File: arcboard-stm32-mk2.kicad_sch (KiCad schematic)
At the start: 92 parts, among them J1 Conn_01x04_Socket, J17 Conn_01x04_Socket, J2 Conn_01x04_Socket, J3 Conn_01x04_Socket, J4 Conn_01x02_Socket, J5 Conn_01x02_Socket, J6 Conn_01x02_Socket, J7 Conn_01x02_Socket, J8 Conn_01x02_Socket, U1 XC6210B332MR-G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

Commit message: refactoring rgb-lcd power to match tzarc, old way was fundamentally broken
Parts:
- removed JP1, JP4: SolderJumper_3_Open, Jumper:SolderJumper-3_P1.3mm_Open_RoundedPad1.0x1.5mm, symbol Jumper:SolderJumper_3_Open
- removed MOSFET2: AO3401A, kicad-libraries:SOT-23_L2.9-W1.3-P1.90-LS2.4-BR, symbol kicad-libraries:AO3401A
- removed R7, R8: 10k, Resistor_SMD:R_0402_1005Metric, symbol Device:R
- added MOSFET4: AO3401A, kicad-libraries:SOT-23_L2.9-W1.3-P1.90-LS2.4-BR, symbol kicad-libraries:AO3401A
- added U10, U9: MMUN2233LT1G, kicad-libraries:SOT-23-3_L2.9-W1.3-P1.90-LS2.4-BR, symbol kicad-libraries:MMUN2233LT1G
- D1: LCSC (none) -> C8678
- J4, J8, U7: now left out of the parts list
- U2: LCSC (none) -> C12345
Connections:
- net +5V: now also MOSFET4.2 (S)
- net GND: now also U10.2 (E), U9.2 (E)
- net LCD_ON: now also U9.1 (B)
- net RGB_5V: now also MOSFET4.3 (D)
- net RGB_ON: now also U10.1 (B)
- net at MOSFET3.1 (G): now also U9.3 (C)
- new net: MOSFET4.1 (G), U10.3 (C)
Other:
- note removed: "v1.1: Moved from 8mhz to 12mhz crystal, to satisfy QMK defaults."
- moved on the sheet: MOSFET3, Y1

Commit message: silkscreen refactoring and moving bits around
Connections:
- no-connect marks 34 -> 36
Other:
- moved on the sheet: MOSFET3, MOSFET4, U10, U9

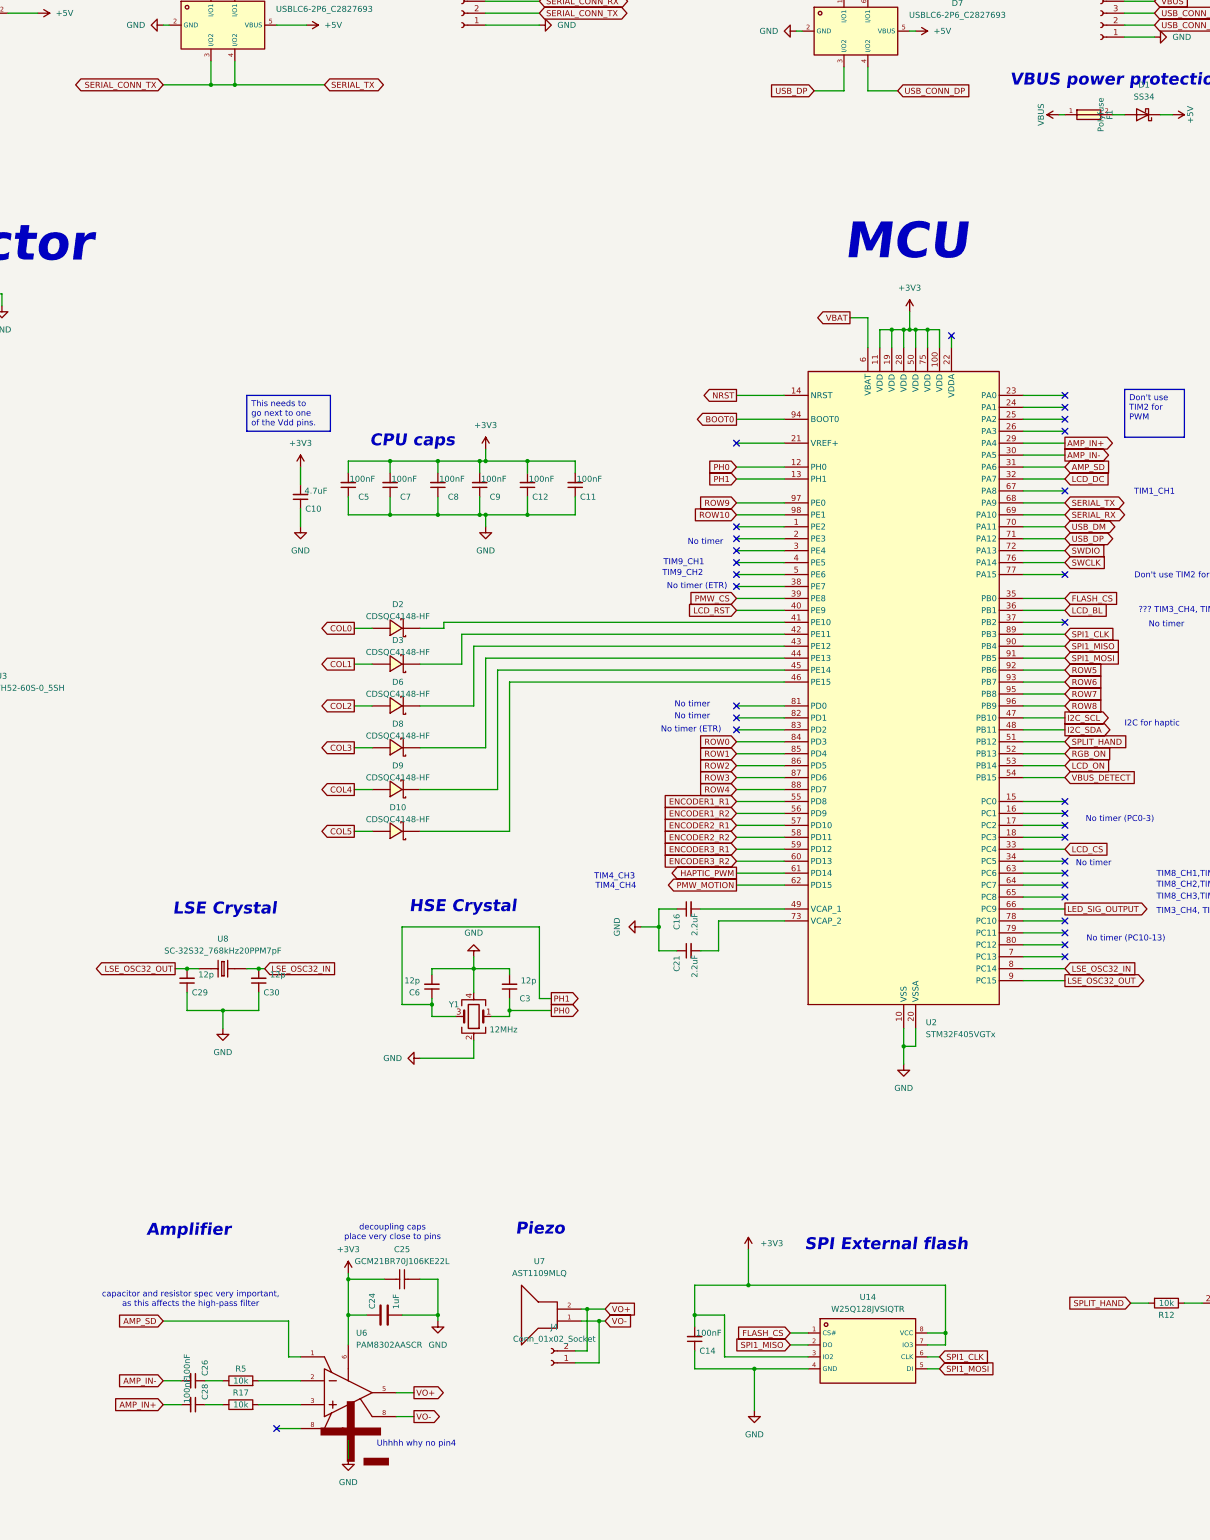
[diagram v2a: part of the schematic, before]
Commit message: improved polyfuse part, fixing critical amplifier symbol mistake, other re-ordering
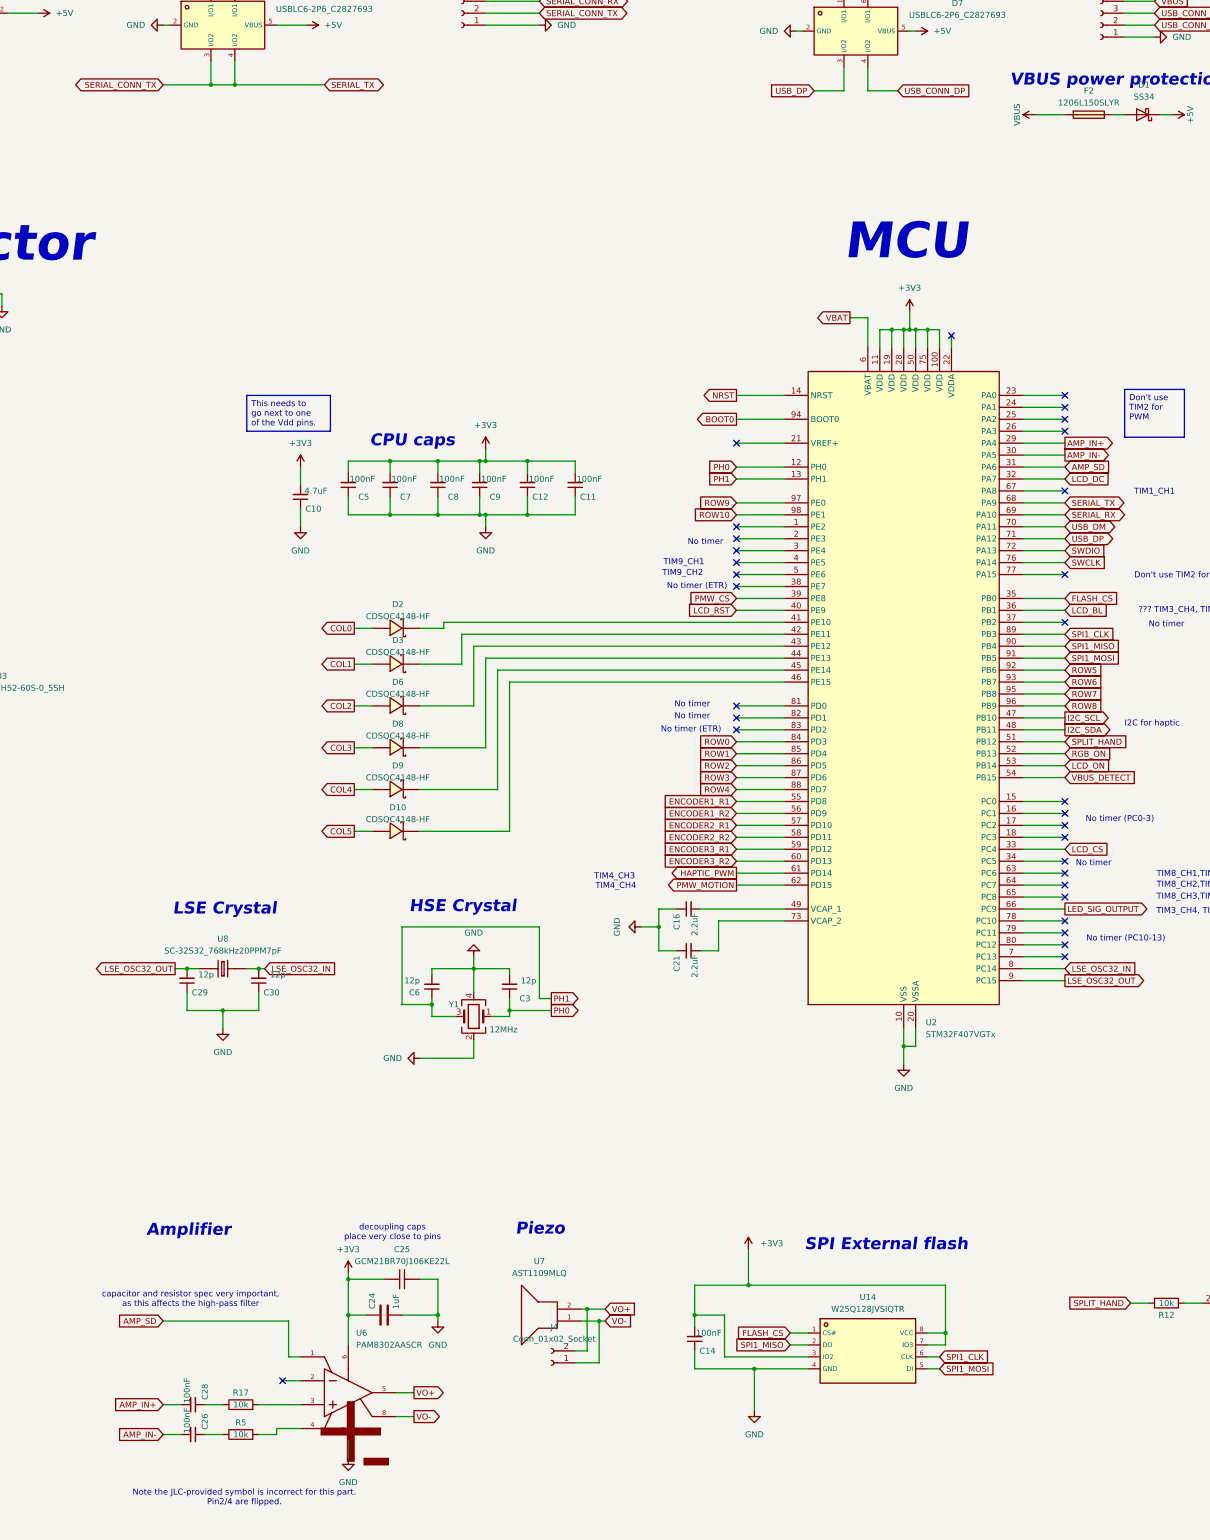
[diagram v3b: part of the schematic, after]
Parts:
- removed F1: Polyfuse, kicad-libraries:F1206, symbol ct-kicad:RF1989-000
- added F2: 1206L150SLYR, kicad-libraries:F1206, symbol kicad-libraries:1206L150SLYR
- U2: value STM32F405VGTx -> STM32F407VGTx
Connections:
- net VBUS: now also F2.1
- net at D1.2 (A): now also F2.2
- net at R5.2: now also U6.4 (IN-); no longer U6.2 (IN-)
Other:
- note added: "Note the JLC-provided symbol is incorrect for this part. Pin2/4 are flipped."
- note removed: "Uhhhh why no pin4"
- moved on the sheet: C26, R5

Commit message: almost ready for ordering
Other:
- note added: "TIM3_CH4, TIM8_CH3N, TIM1_CH3N"
- note removed: "??? TIM3_CH4, TIM8_CH3N, TIM1_CH3N"
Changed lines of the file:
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@@
 		)
 	)
-	(text "??? TIM3_CH4, TIM8_CH3N, TIM1_CH3N"
+	(text "TIM3_CH4, TIM8_CH3N, TIM1_CH3N"
 		(exclude_from_sim no)
 		(at 379.476 204.47 0)

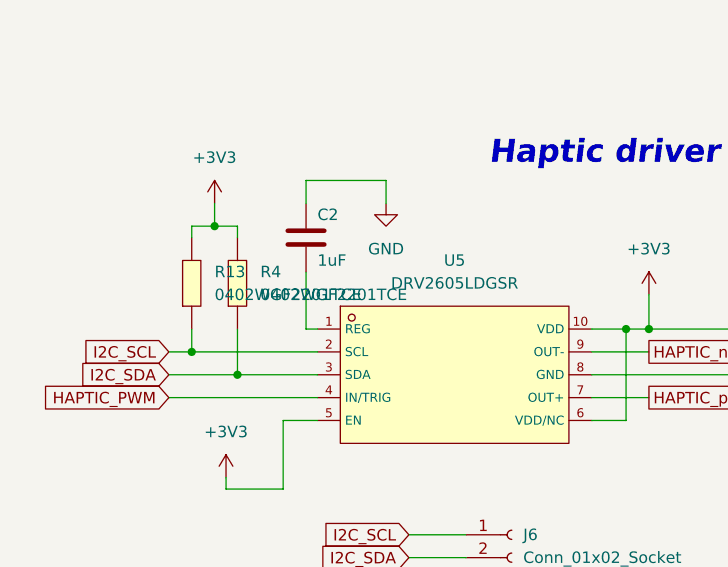
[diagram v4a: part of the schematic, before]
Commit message: fixing i2c resistors, prepping for 10pin
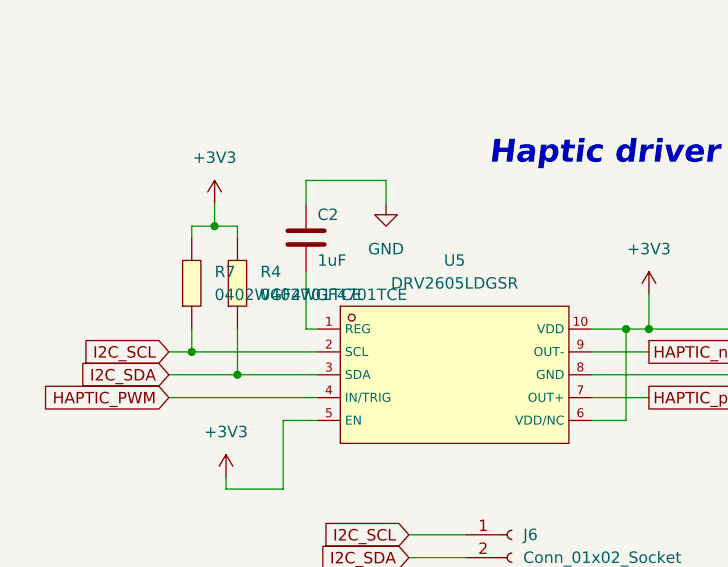
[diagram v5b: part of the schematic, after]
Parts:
- removed R13, R4: 0402WGF2201TCE, kicad-libraries:R0402, symbol kicad-libraries:0402WGF2201TCE
- added R4, R7: 0402WGF4701TCE, kicad-libraries:R0402, symbol kicad-libraries:0402WGF4701TCE
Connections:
- net +3V3: now also R4.2, R7.2
- net I2C_SCL: now also R7.1
- net I2C_SDA: now also R4.1
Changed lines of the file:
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@@
 	)
 	(symbol
+		(lib_id "kicad-libraries:0402WGF4701TCE")
+		(at 53.34 350.52 90)
+		(unit 1)
+		(exclude_from_sim no)
+		(in_bom yes)
+		(on_board yes)
+		(dnp no)
+		(fields_autoplaced yes)
+		(property "Reference" "R4"
+			(at 55.88 349.2499 90)
+			(effects
+				(font
+					(size 1.27 1.27)
+				)
+				(justify right)
+			)
+		)
+		(property "Value" "0402WGF4701TCE"
+			(at 55.88 351.7899 90)
+			(effects
+				(font
+					(size 1.27 1.27)
+				)
+				(justify right)
+			)
+		)
+		(property "Footprint" "kicad-libraries:R0402"
+			(at 63.5 350.52 0)
+			(effects
+				(font
+					(size 1.27 1.27)
+					(italic yes)
+				)
+				(hide yes)
+			)
+		)
+		(property "Datasheet" "https://item.szlcsc.com/323315.html"
+			(at 53.213 352.806 0)
+			(effects
+				(font
+					(size 1.27 1.27)
+				)
+				(justify left)
+				(hide yes)
+			)
+		)
+		(property "Description" ""
+			(at 53.34 350.52 0)
+			(effects
+				(font
+					(size 1.27 1.27)
+				)
+				(hide yes)
+			)
+		)
+		(property "LCSC" "C25900"
+			(at 53.34 350.52 0)
+			(effects
+				(font
+					(size 1.27 1.27)
+				)
+				(hide yes)
+			)
+		)
+		(pin "2"
+		)
+		(pin "1"
+		)
+		(instances
+			(project "arcboard-stm32-mk2"
+				(path "/e3b5a64c-dc86-4c04-b1b0-762b30a6a8fe"
+					(reference "R4")
+					(unit 1)
+				)
+			)
+		)
+	)
+	(symbol
 		(lib_id "kicad-libraries:AO3401A")
 		(at 504.19 260.35 0)
@@
 	)
 	(symbol
-		(lib_id "kicad-libraries:0402WGF2201TCE")
-		(at 48.26 350.52 90)
-		(unit 1)
-		(exclude_from_sim no)
-		(in_bom yes)
-		(on_board yes)
-		(dnp no)
-		(fields_autoplaced yes)
-		(property "Reference" "R13"
-			(at 50.8 349.2499 90)
-			(effects
-				(font
-					(size 1.27 1.27)
-				)
-				(justify right)
-			)
-		)
-		(property "Value" "0402WGF2201TCE"
-			(at 50.8 351.7899 90)
-			(effects
-				(font
-					(size 1.27 1.27)
-				)
-				(justify right)
-			)
-		)
-		(property "Footprint" "kicad-libraries:R0402"
-			(at 58.42 350.52 0)
-			(effects
-				(font
-					(size 1.27 1.27)
-					(italic yes)
-				)
-				(hide yes)
-			)
-		)
-		(property "Datasheet" "https://item.szlcsc.com/323315.html"
-			(at 48.133 352.806 0)
-			(effects
-				(font
-					(size 1.27 1.27)
-				)
-				(justify left)
-				(hide yes)
-			)
-		)
-		(property "Description" ""
-			(at 48.26 350.52 0)
-			(effects
-				(font
-					(size 1.27 1.27)
-				)
-				(hide yes)
-			)
-		)
-		(property "LCSC" "C25879"
-			(at 48.26 350.52 0)
-			(effects
-				(font
-					(size 1.27 1.27)
-				)
-				(hide yes)
-			)
-		)
-		(pin "2"
-		)
-		(pin "1"
-		)
-		(instances
-			(project ""
-				(path "/e3b5a64c-dc86-4c04-b1b0-762b30a6a8fe"
-					(reference "R13")
-					(unit 1)
-				)
-			)
-		)
-	)
-	(symbol
 		(lib_id "kicad-libraries:CL10A106MA8NRNC")
 		(at 519.43 63.5 270)
@@
 	)
 	(symbol
+		(lib_id "kicad-libraries:0402WGF4701TCE")
+		(at 48.26 350.52 90)
+		(unit 1)
+		(exclude_from_sim no)
+		(in_bom yes)
+		(on_board yes)
+		(dnp no)
+		(fields_autoplaced yes)
+		(property "Reference" "R7"
+			(at 50.8 349.2499 90)
+			(effects
+				(font
+					(size 1.27 1.27)
+				)
+				(justify right)
+			)
+		)
+		(property "Value" "0402WGF4701TCE"
+			(at 50.8 351.7899 90)
+			(effects
+				(font
+					(size 1.27 1.27)
+				)
+				(justify right)
+			)
+		)
+		(property "Footprint" "kicad-libraries:R0402"
+			(at 58.42 350.52 0)
+			(effects
+				(font
+					(size 1.27 1.27)
+					(italic yes)
+				)
+				(hide yes)
+			)
+		)
+		(property "Datasheet" "https://item.szlcsc.com/323315.html"
+			(at 48.133 352.806 0)
+			(effects
+				(font
+					(size 1.27 1.27)
+				)
+				(justify left)
+				(hide yes)
+			)
+		)
+		(property "Description" ""
+			(at 48.26 350.52 0)
+			(effects
+				(font
+					(size 1.27 1.27)
+				)
+				(hide yes)
+			)
+		)
+		(property "LCSC" "C25900"
+			(at 48.26 350.52 0)
+			(effects
+				(font
+					(size 1.27 1.27)
+				)
+				(hide yes)
+			)
+		)
+		(pin "2"
+		)
+		(pin "1"
+		)
+		(instances
+			(project ""
+				(path "/e3b5a64c-dc86-4c04-b1b0-762b30a6a8fe"
+					(reference "R7")
+					(unit 1)
+				)
+			)
+		)
+	)
+	(symbol
 		(lib_id "Device:C_Small")
 		(at 161.29 373.38 270)
@@
 					(unit 1)
 				)
-			)
-		)
-	)
-	(symbol
-		(lib_id "kicad-libraries:0402WGF2201TCE")
-		(at 53.34 350.52 90)
-		(unit 1)
-		(exclude_from_sim no)
-		(in_bom yes)
-		(on_board yes)
-		(dnp no)
-		(fields_autoplaced yes)
-		(property "Reference" "R4"
-			(at 55.88 349.2499 90)
-			(effects
-				(font
-					(size 1.27 1.27)
-				)
-				(justify right)
-			)
-		)
-		(property "Value" "0402WGF2201TCE"
-			(at 55.88 351.7899 90)
-			(effects
-				(font
-					(size 1.27 1.27)
-				)
-				(justify right)
-			)
-		)
-		(property "Footprint" "kicad-libraries:R0402"
-			(at 63.5 350.52 0)
-			(effects
-				(font
-					(size 1.27 1.27)
-					(italic yes)
-				)
-				(hide yes)
-			)
-		)
-		(property "Datasheet" "https://item.szlcsc.com/323315.html"
-			(at 53.213 352.806 0)
-			(effects
-				(font
-					(size 1.27 1.27)
-				)
-				(justify left)
-				(hide yes)
-			)
-		)
-		(property "Description" ""
-			(at 53.34 350.52 0)
-			(effects
-				(font
-					(size 1.27 1.27)
-				)
-				(hide yes)
-			)
-		)
-		(property "LCSC" "C25879"
-			(at 53.34 350.52 0)
-			(effects
-				(font
-					(size 1.27 1.27)
-				)
-				(hide yes)
-			)
-		)
-		(pin "2"
-		)
-		(pin "1"
-		)
-		(instances
-			(project "arcboard-stm32-mk2"
-				(path "/e3b5a64c-dc86-4c04-b1b0-762b30a6a8fe"
-					(reference "R4")
-					(unit 1)
-				)

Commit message: bunch o updates
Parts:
- removed J3: Conn_01x04_Socket, Connector_JST:JST_PH_S4B-PH-K_1x04_P2.00mm_Horizontal, symbol Connector:Conn_01x04_Socket
- removed J5, J7, J8: Conn_01x02_Socket, Connector_JST:JST_PH_S2B-PH-K_1x02_P2.00mm_Horizontal, symbol Connector:Conn_01x02_Socket
- added J3, J5, J7: Conn_01x01, TestPoint:TestPoint_Pad_1.5x1.5mm, symbol Connector_Generic:Conn_01x01
- added J9: Conn_01x10_Socket, Connector_JST:JST_PH_S10B-PH-K_1x10_P2.00mm_Horizontal, symbol Connector:Conn_01x10_Socket
- added R8: 0402WGF4701TCE, kicad-libraries:R0402, symbol kicad-libraries:0402WGF4701TCE
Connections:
- net +3V3: now also J9.5 (Pin_5), R8.2
- net GND: now also C1.1, J9.1 (Pin_1), J9.6 (Pin_6); no longer C1.2
- net HAPTIC_neg: now also J9.9 (Pin_9)
- net HAPTIC_pos: now also J9.10 (Pin_10)
- net LED_EXT_DI: now also J9.3 (Pin_3)
- net RGB_5V: now also C1.2, J9.2 (Pin_2); no longer C1.1
- net VBAT: now also J9.8 (Pin_8)
- net DFU: now reaches D11.2 (A), R15.1, U15.4 (D)
- net DFU: now also J9.4 (Pin_4)
- net LIMIT1: now reaches U2.63 (PC6)
- net LIMIT1: now also J9.7 (Pin_7), R8.1
- net SPARE1: now reaches U2.64 (PC7)
- net SPARE1: now also J3.1 (Pin_1)
- net SPARE2: now reaches U2.65 (PC8)
- net SPARE2: now also J5.1 (Pin_1)
- net SPARE3: now reaches U2.67 (PA8)
- net SPARE3: now also J7.1 (Pin_1)
- no-connect marks 36 -> 31
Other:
- note added: "Outputs"
- note added: "Spare pins"
- note added: "Wiring harness"
- note removed: "External VBAT"
- note removed: "Other outputs"
- note removed: "RGB LED chain output"
- moved on the sheet: C1, J2, MOSFET3, MOSFET4, U10, U9
